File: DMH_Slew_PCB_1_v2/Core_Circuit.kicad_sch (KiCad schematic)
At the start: 45 parts, among them J1 TS_Jack_6.35mm_Sw, J2 TS_Jack_6.35mm_Sw, J3 TS_Jack_6.35mm_Sw, Q1 BC548, Q2 BC548, Q3 BC558, Q4 BC558, SW1 SW_DPDT_3way, SW2 SW_DPDT, U1 TL072, U2 TL074

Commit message: Notes while breadboarding
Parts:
- added R29: 100k, Resistor_THT:R_Axial_DIN0207_L6.3mm_D2.5mm_P7.62mm_Horizontal, symbol Device:R_US
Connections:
- net GND: now also U2.5 (+), R29.2; no longer J2.TN, U2.10 (+)
- net Output: no longer R26.2, U2.8
- net at R3.2, RV1.3: now also SW1.5 (B); no longer SW1.2 (B)
- net at R4.2, RV2.3: now also SW1.2 (B); no longer SW1.5 (B)
- net at C9.1, Q2.1 (C), Q3.1 (C): now also U2.6 (-); no longer U2.9 (-)
- new net: J2.TN, R29.1
- new net: R26.2, U2.7
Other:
- note added: "22pF in bb"
- note added: "2x 100nF in bb"
- note added: "2x SPST switches"
- moved on the sheet: C8, R17, R18, R19, SW1, U2D

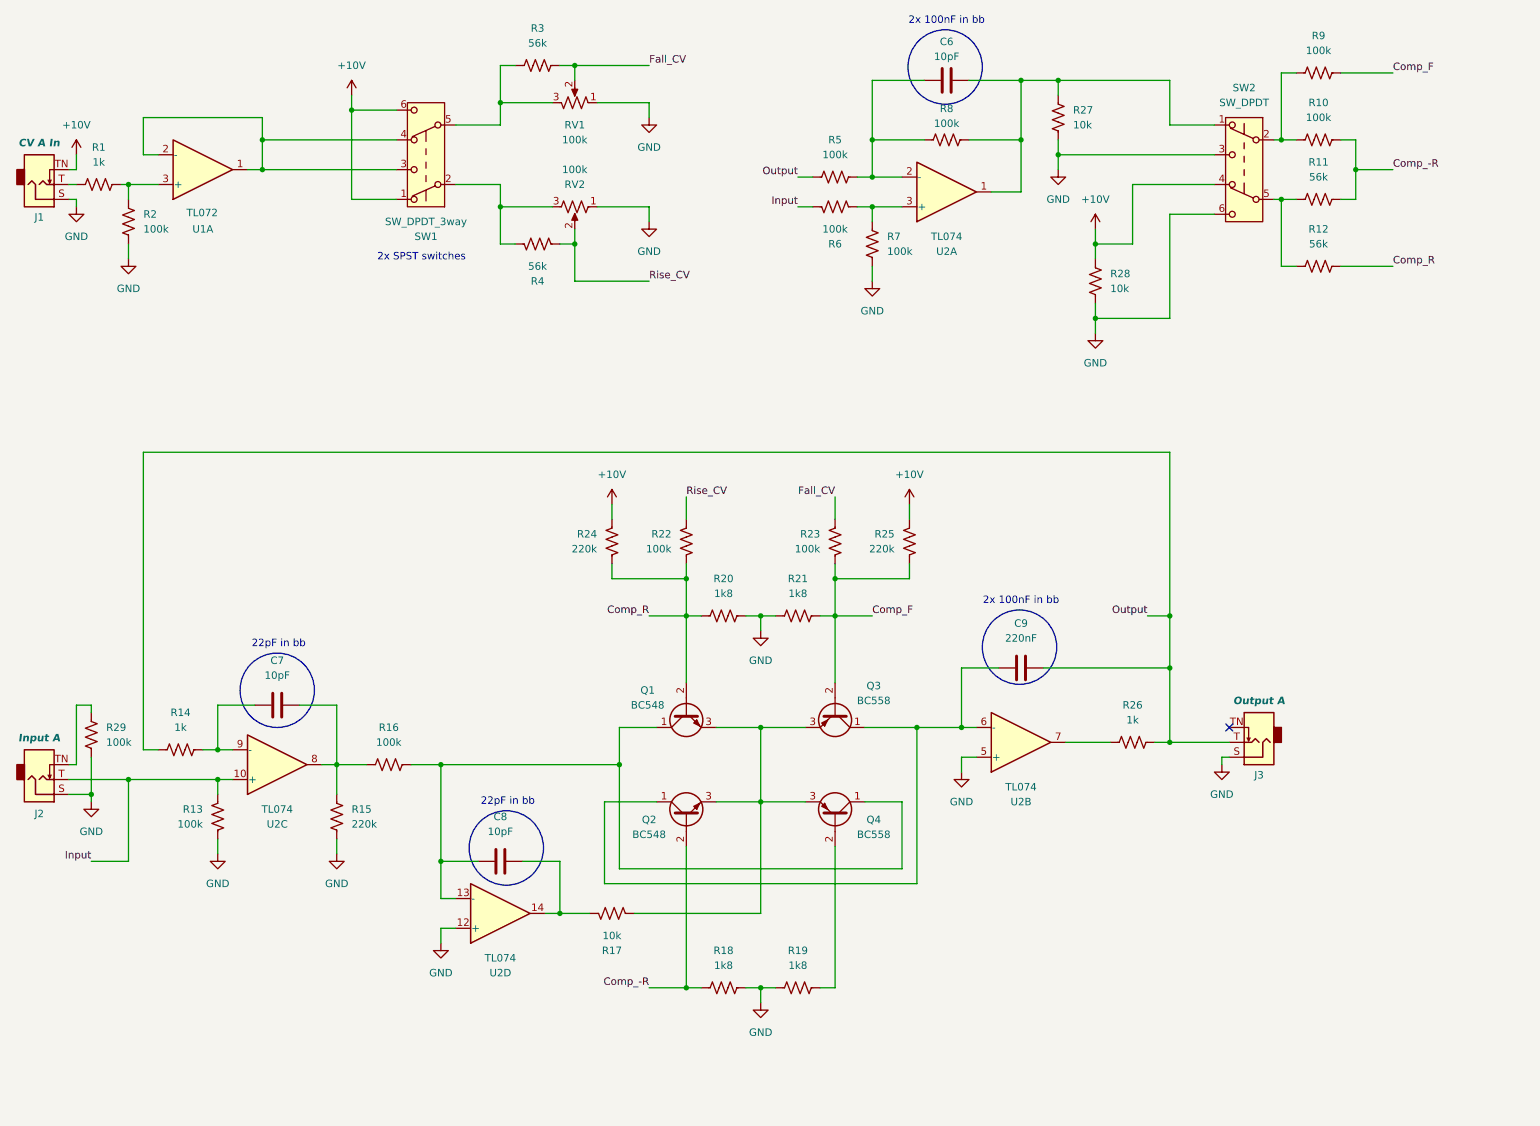
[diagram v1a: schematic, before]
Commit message: Added state gate outputs circuit
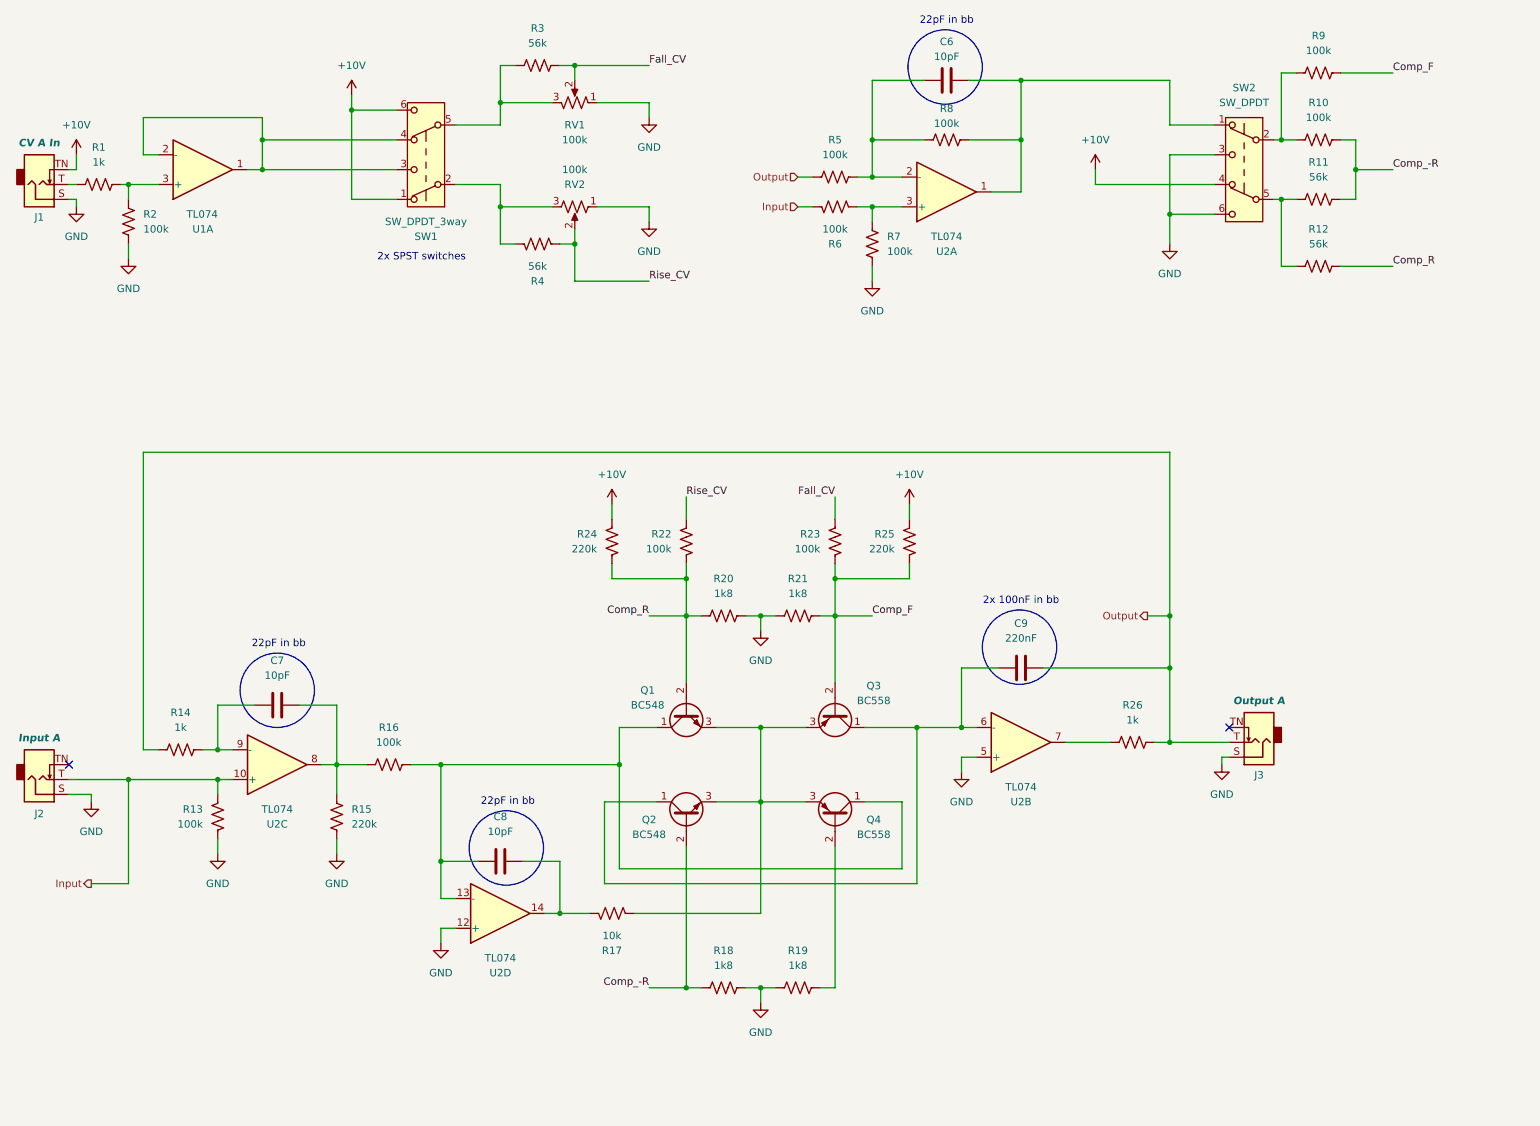
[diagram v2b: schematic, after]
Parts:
- removed R27, R28: 10k, Resistor_THT:R_Axial_DIN0207_L6.3mm_D2.5mm_P7.62mm_Horizontal, symbol Device:R_US
- removed R29: 100k, Resistor_THT:R_Axial_DIN0207_L6.3mm_D2.5mm_P7.62mm_Horizontal, symbol Device:R_US
- U1: value TL072 -> TL074; footprint Package_DIP:DIP-8_W7.62mm_Socket -> Package_DIP:DIP-16_W7.62mm_Socket; symbol Amplifier_Operational:TL072 -> Amplifier_Operational:TL074
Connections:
- no-connect marks 1 -> 2

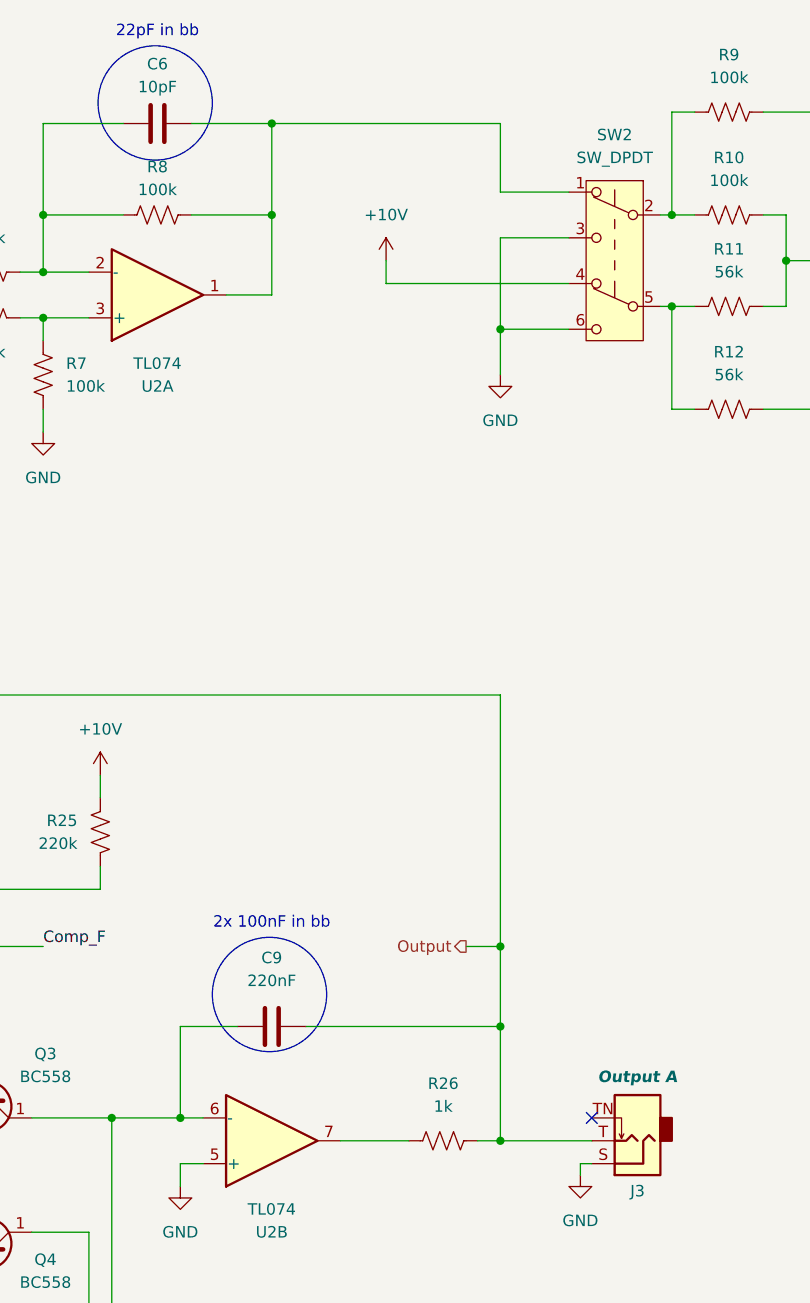
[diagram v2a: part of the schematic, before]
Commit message: Added alternative range capacitors and switch
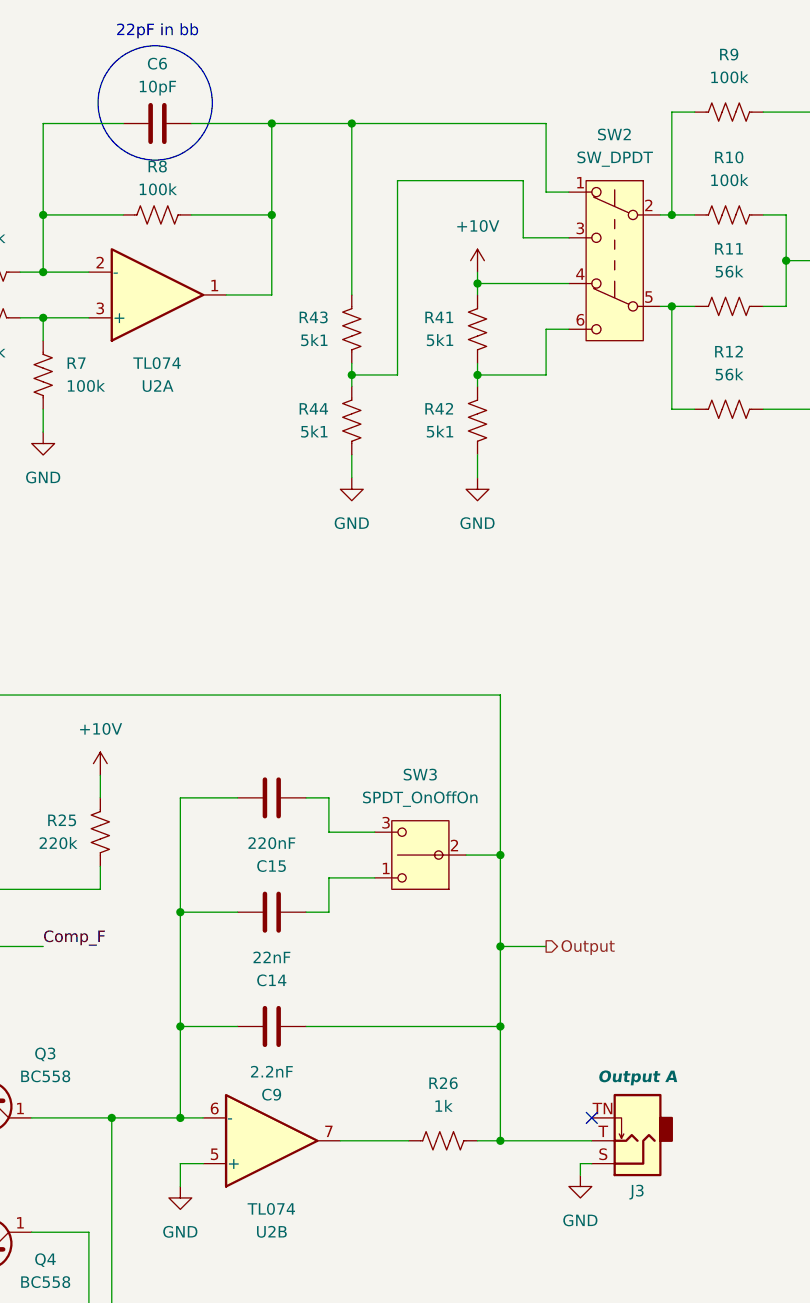
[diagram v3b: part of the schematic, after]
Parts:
- added C14: 22nF, Capacitor_THT:C_Disc_D4.3mm_W1.9mm_P5.00mm, symbol Device:C
- added C15: 220nF, Capacitor_THT:C_Disc_D4.3mm_W1.9mm_P5.00mm, symbol Device:C
- added R41, R42, R43, R44: 5k1, Resistor_THT:R_Axial_DIN0207_L6.3mm_D2.5mm_P7.62mm_Horizontal, symbol Device:R_US
- added SW3: SPDT_OnOffOn, SynthStuff:Toggle_Switch_TE, symbol SynthStuff:SW_SPDT_OnOffOn
- C9: value 220nF -> 2.2nF
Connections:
- net +10V: now also R41.1
- net GND: now also R42.2, R44.2; no longer SW2.3 (C), SW2.6 (C)
- net Output: now also SW3.2 (B)
- net at C6.2, R8.1, SW2.1 (A)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: now also R43.1
- net at C9.1, Q2.1 (C), Q3.1 (C)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: now also C14.1, C15.1
- new net: C15.2, SW3.3 (C)
- new net: R43.2, R44.1, SW2.3 (C)
- new net: R41.2, R42.1, SW2.6 (C)
- new net: C14.2, SW3.1 (A)
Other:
- note removed: "2x 100nF in bb"

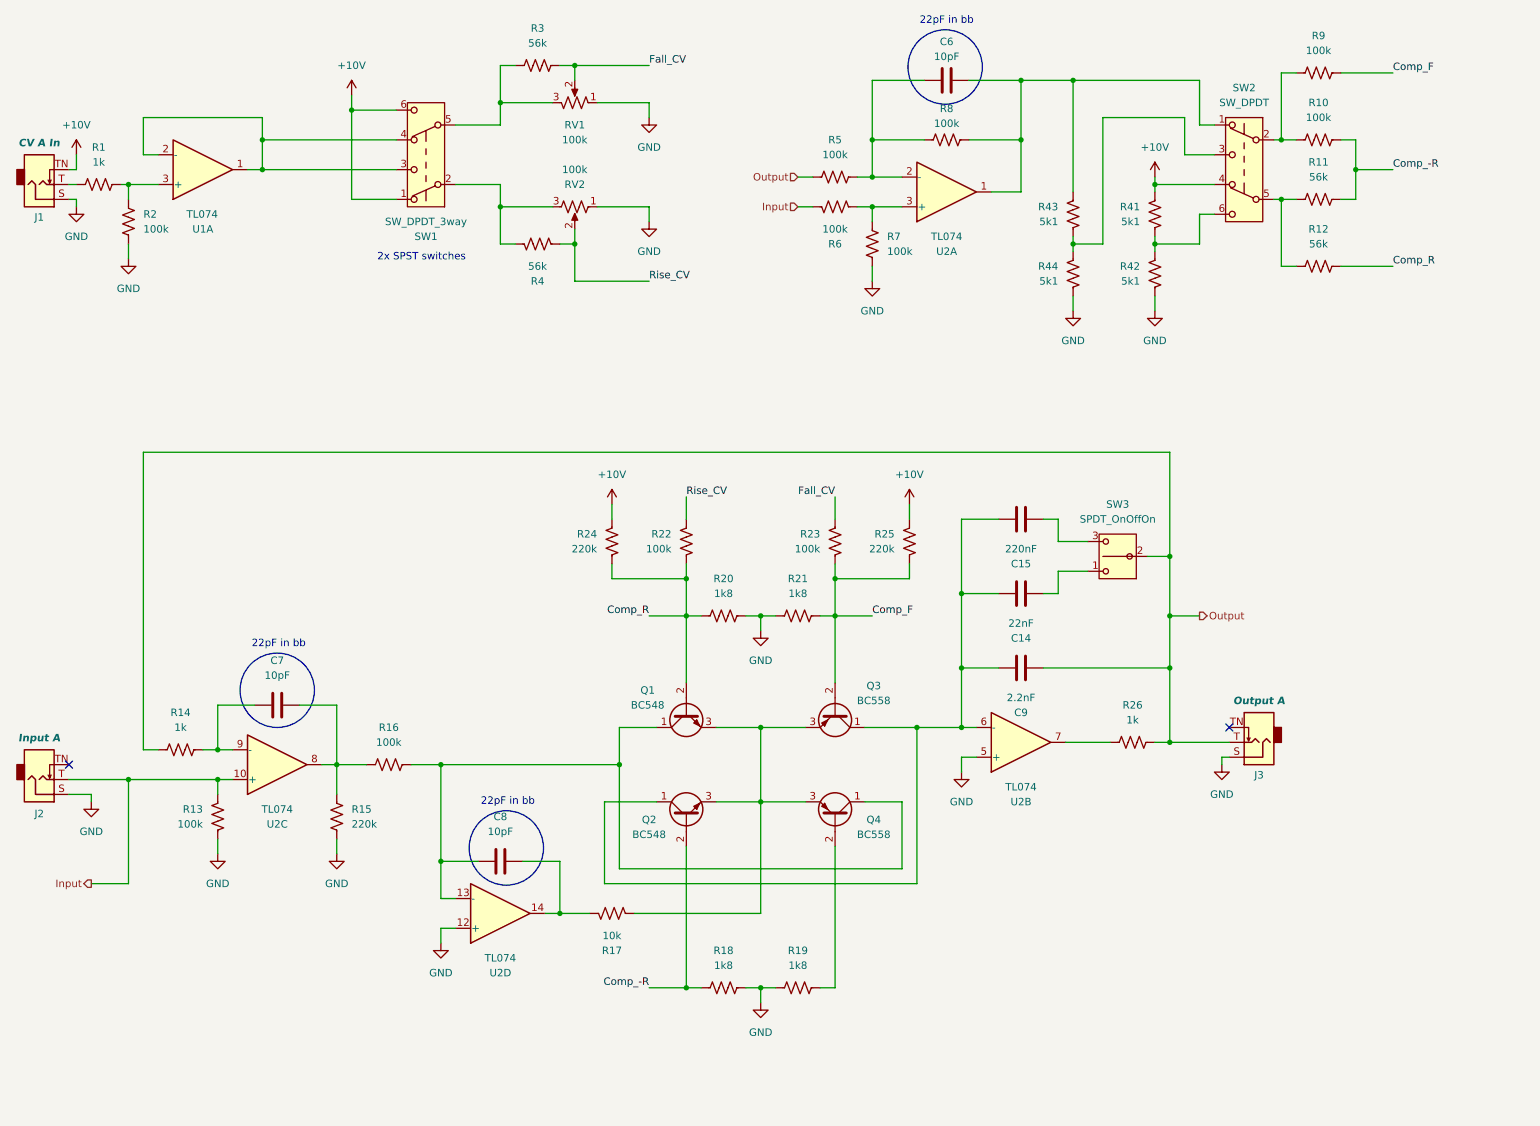
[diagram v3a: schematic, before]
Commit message: Separating PCB 1 and 2 in schematic
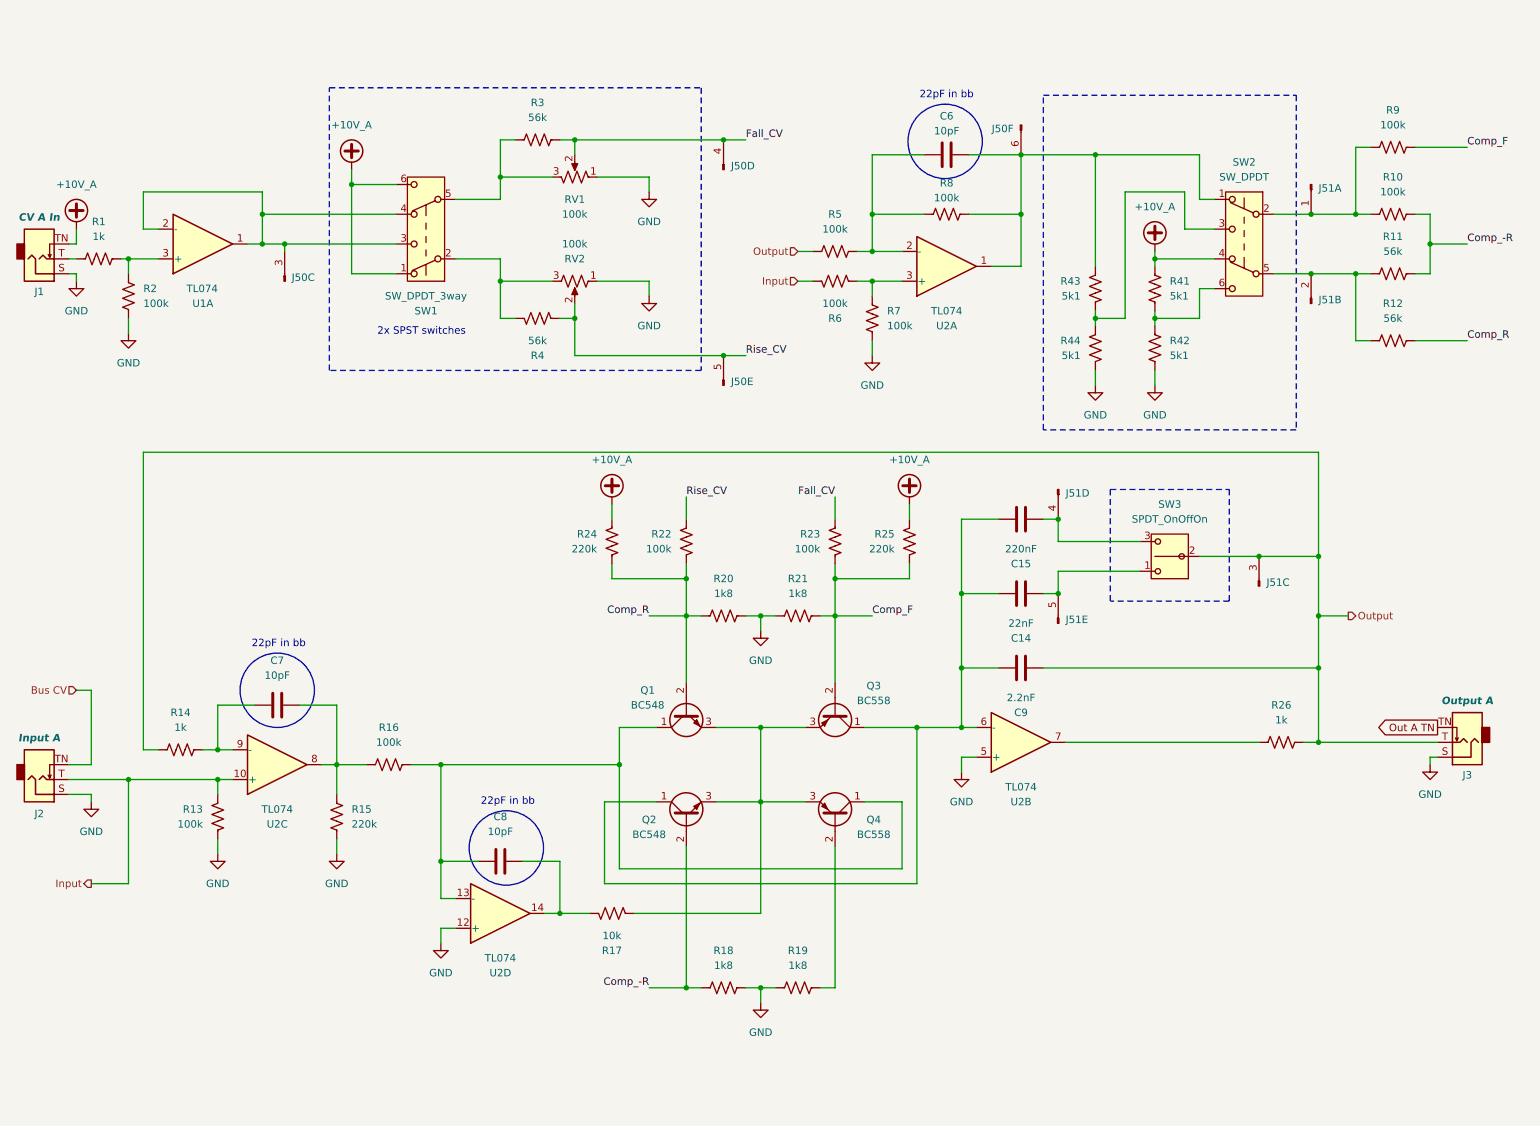
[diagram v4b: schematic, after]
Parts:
- added J50, J51: Conn_01x08_PinHeader, Connector_PinHeader_2.54mm:PinHeader_1x08_P2.54mm_Vertical, symbol SynthStuff:Conn_01x08_PinHeader
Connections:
- net Fall_CV: now also J50.4 (Pin_4)
- net Output: now also J51.3 (Pin_3)
- net Rise_CV: now also J50.5 (Pin_5)
- net at C15.2, SW3.3 (C): now also J51.4 (Pin_4)
- net at C6.2, R43.1, R8.1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: now also J50.6 (Pin_6)
- net at SW1.3 (C), SW1.4 (A), U1.1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: now also J50.3 (Pin_3)
- net at R10.2, R9.2, SW2.2 (B): now also J51.1 (Pin_1)
- net at R11.2, R12.2, SW2.5 (B): now also J51.2 (Pin_2)
- net Out A TN: now reaches J3.TN
- net at C14.2, SW3.1 (A): now also J51.5 (Pin_5)
- net Bus CV: now reaches J2.TN
- net +10V renamed +10V_A
- no-connect marks 2 -> 0
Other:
- moved on the sheet: C6, J1, J3, R1, R10, R11, R12, R2, R26, R3, R4, R41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
